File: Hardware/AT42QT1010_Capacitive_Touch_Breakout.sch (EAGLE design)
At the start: 30 parts, among them Q1 NPN, U1 AT42QT1010UDFN

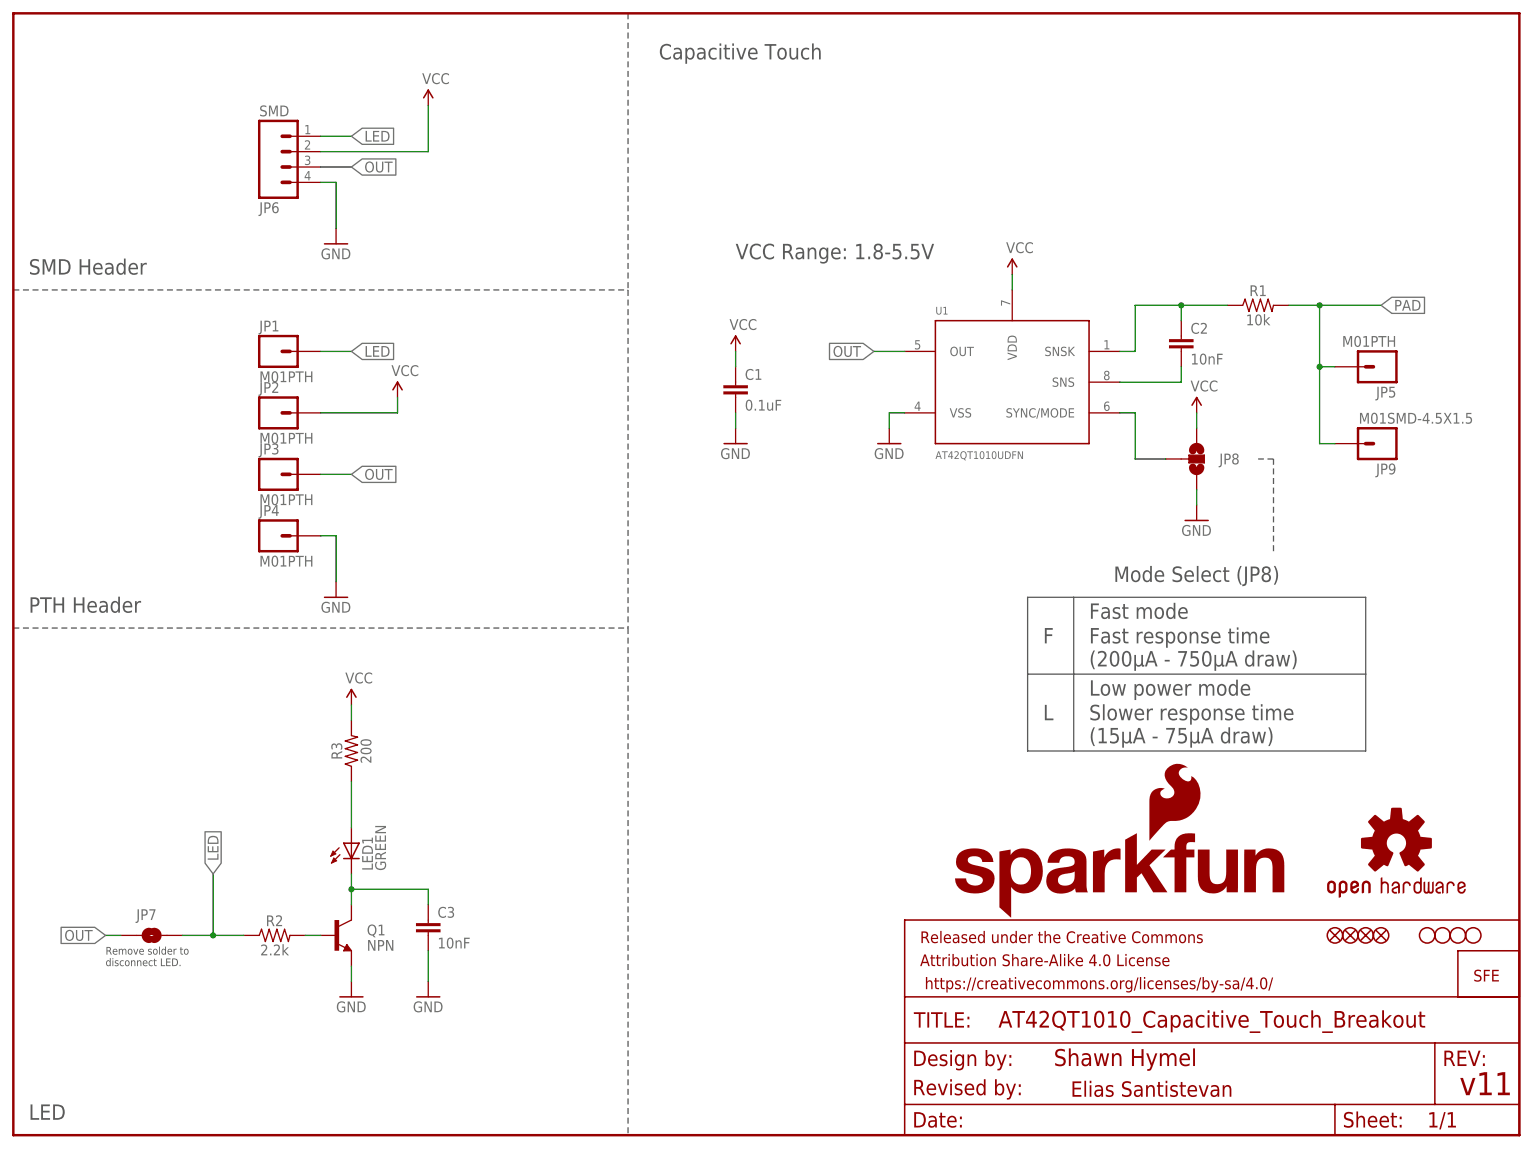
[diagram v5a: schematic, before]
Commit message: Update from Review Feedback
Added better text to the schematic to explain slow/fast mode. Got rid of
an uneccesary VCC trace, added more gnd vias and changed all vias to 15
mil for consistency.
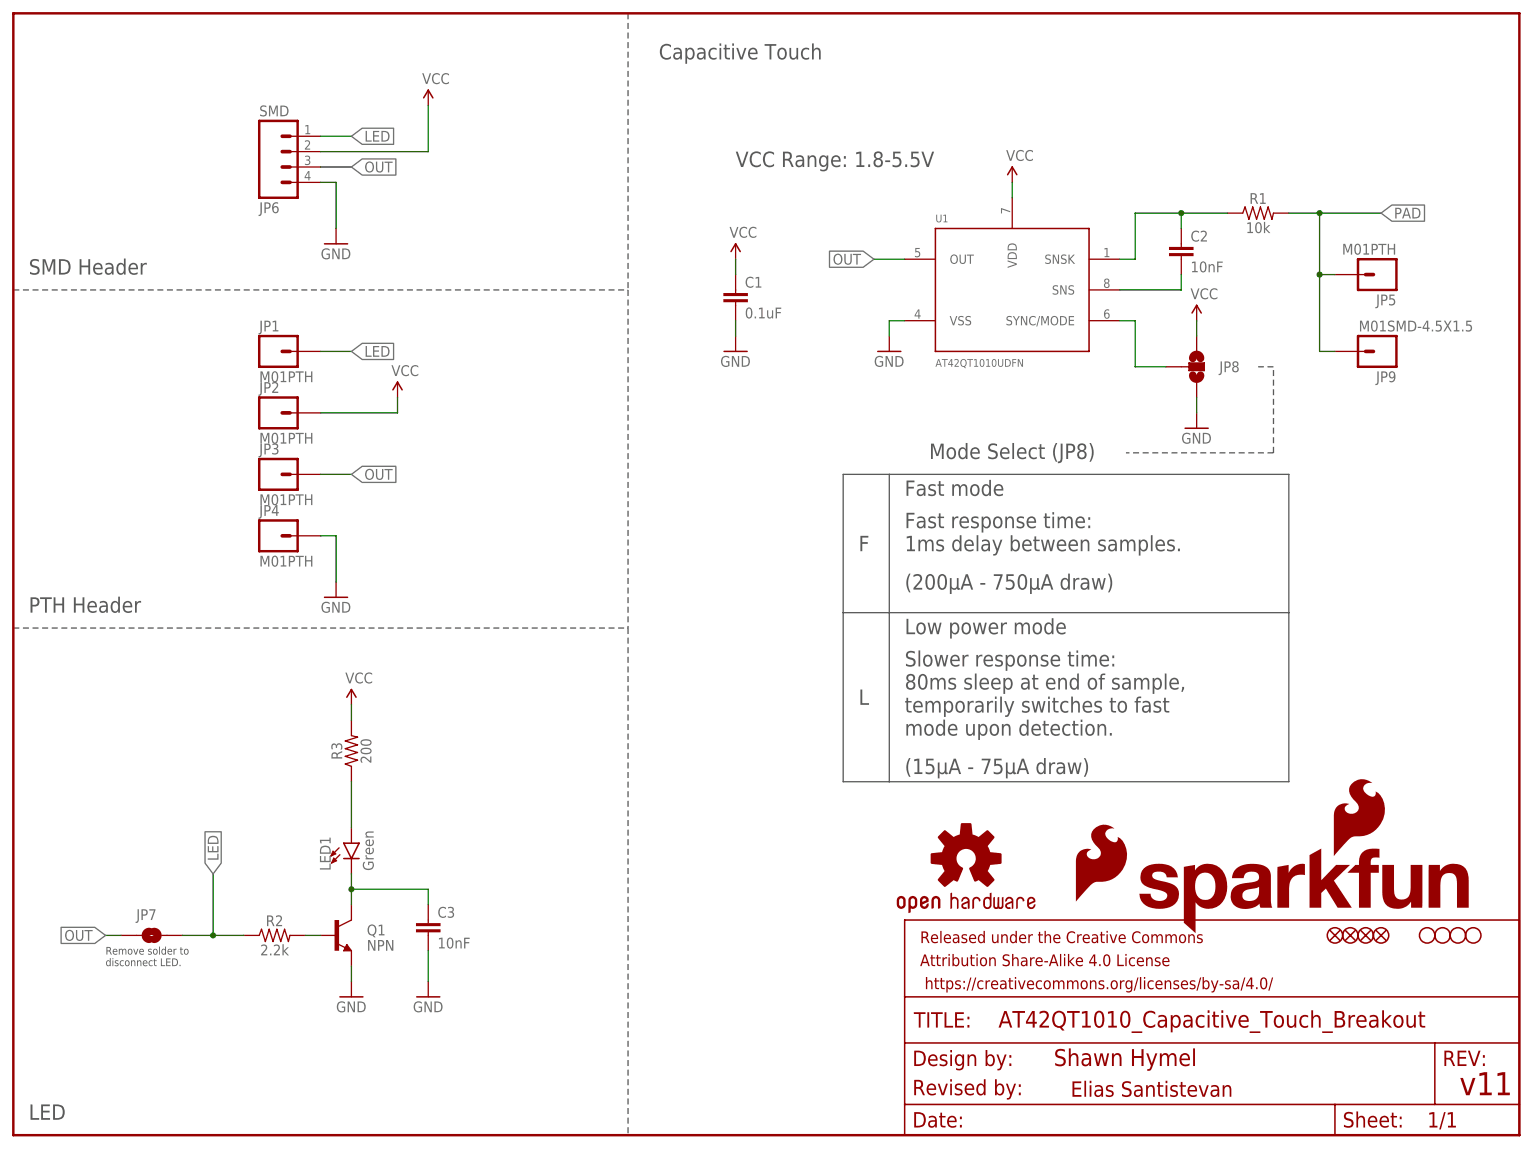
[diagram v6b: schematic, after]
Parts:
- removed LOGO3: LOGO-SFESK, SparkFun-Aesthetics:LOGO-SFESK
- added LOGO1: SFE_LOGO_FLAME.3_INCH, SparkFun-Aesthetics:SFE_LOGO_FLAME.3_INCH
- LED1: value GREEN -> Green; device SparkFun-LED:LED1206-BOTTOM -> SparkFun-LED:LED-GREEN1206-BOTTOM
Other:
- note added: "Fast response time: 1ms delay between samples."
- note added: "Slower response time: 80ms sleep at end of sample, temporarily switches to fast mode upon detection."
- note removed: "Fast response time"
- note removed: "Slower response time"
- moved on the sheet: C1, C2, JP5, JP8, JP9, R1, U1
